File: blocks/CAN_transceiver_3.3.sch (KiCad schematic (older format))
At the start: 0 parts

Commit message: added 4.4v can transciever
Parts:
- added C?: 100n, symbol Device:C
- added U?: SN65HVD232, Package_SO:SOIC-8_3.9x4.9mm_P1.27mm, symbol Interface_CAN_LIN:SN65HVD232
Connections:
- new net +3V3: C?.2, U?.3 (VCC)
- new net CANH: U?.7 (CANH)
- new net CANL: U?.6 (CANL)
- new net GND: C?.1, U?.2 (GND)
- new net RX: U?.4 (R)
- new net TX: U?.1 (D)
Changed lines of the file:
@@
 EESchema Schematic File Version 4
-LIBS:blocks-cache
-EELAYER 29 0
+EELAYER 30 0
 EELAYER END
 $Descr A4 11693 8268
@@
 Comment4 ""
 $EndDescr
+$Comp
+L Interface_CAN_LIN:SN65HVD232 U?
+U 1 1 5EEB2C8B
+P 5500 3000
+F 0 "U?" H 5300 3250 50  0000 C CNN
+F 1 "SN65HVD232" H 5850 2650 50  0000 C CNN
+F 2 "Package_SO:SOIC-8_3.9x4.9mm_P1.27mm" H 5500 2500 50  0001 C CNN
+F 3 "http://www.ti.com/lit/ds/symlink/sn65hvd230.pdf" H 5400 3400 50  0001 C CNN
+	1    5500 3000
+	1    0    0    -1
+$EndComp
+Text HLabel 4700 2900 0    50   Input ~ 0
+TX
+Text HLabel 4700 3000 0    50   Output ~ 0
+RX
+Wire Wire Line
+	4700 2900 5100 2900
+Wire Wire Line
+	5100 3000 4700 3000
+Text HLabel 6350 3000 2    50   BiDi ~ 0
+CANH
+Text HLabel 6350 3100 2    50   BiDi ~ 0
+CANL
+Wire Wire Line
+	5900 3000 6350 3000
+Wire Wire Line
+	6350 3100 5900 3100
+Wire Wire Line
+	5500 2700 5500 2550
+$Comp
+L power:+3.3V #PWR?
+U 1 1 5EEB36C2
+P 5500 2400
+F 0 "#PWR?" H 5500 2250 50  0001 C CNN
+F 1 "+3.3V" H 5515 2573 50  0000 C CNN
+F 2 "" H 5500 2400 50  0001 C CNN
+F 3 "" H 5500 2400 50  0001 C CNN
+	1    5500 2400
+	1    0    0    -1
+$EndComp
+$Comp
+L power:GND #PWR?
+U 1 1 5EEB3802
+P 5500 3500
+F 0 "#PWR?" H 5500 3250 50  0001 C CNN
+F 1 "GND" H 5505 3327 50  0000 C CNN
+F 2 "" H 5500 3500 50  0001 C CNN
+F 3 "" H 5500 3500 50  0001 C CNN
+	1    5500 3500
+	1    0    0    -1
+$EndComp
+Wire Wire Line
+	5500 3500 5500 3400
+$Comp
+L Device:C C?
+U 1 1 5EEB3AF7
+P 5750 2550
+F 0 "C?" V 5498 2550 50  0000 C CNN
+F 1 "100n" V 5589 2550 50  0000 C CNN
+F 2 "" H 5788 2400 50  0001 C CNN
+F 3 "~" H 5750 2550 50  0001 C CNN
+	1    5750 2550
+	0    1    1    0
+$EndComp
+Wire Wire Line
+	5600 2550 5500 2550
+Connection ~ 5500 2550
+Wire Wire Line
+	5500 2550 5500 2400
+$Comp
+L power:GND #PWR?
+U 1 1 5EEB4720
+P 5950 2600
+F 0 "#PWR?" H 5950 2350 50  0001 C CNN
+F 1 "GND" H 5955 2427 50  0000 C CNN
+F 2 "" H 5950 2600 50  0001 C CNN
+F 3 "" H 5950 2600 50  0001 C CNN
+	1    5950 2600
+	1    0    0    -1
+$EndComp
+Wire Wire Line
+	5950 2600 5950 2550
+Wire Wire Line
+	5950 2550 5900 2550
 $EndSCHEMATC

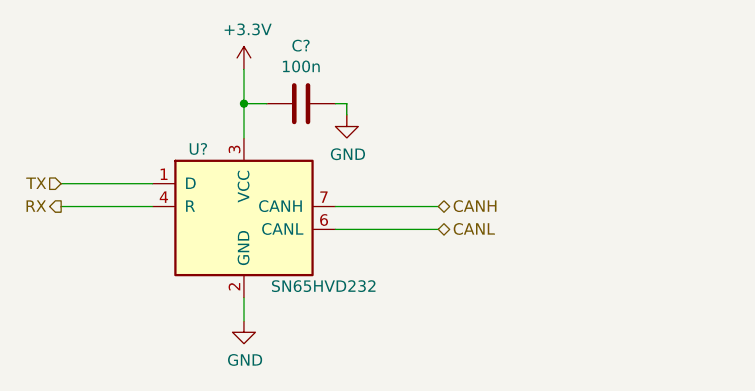
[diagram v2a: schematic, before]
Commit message: changed 3.3 can to sn65hvd233
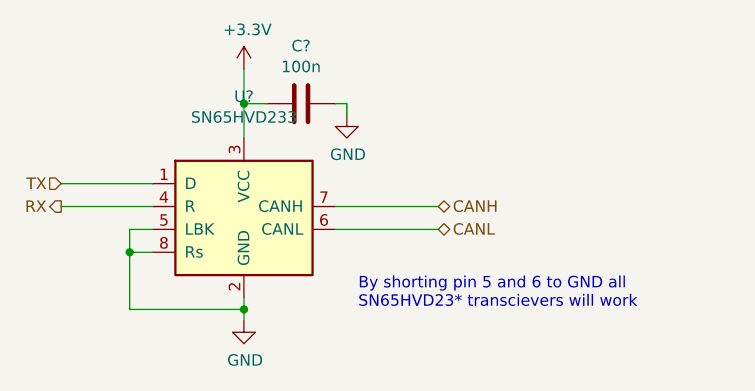
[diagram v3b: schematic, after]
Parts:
- removed U?: SN65HVD232, Package_SO:SOIC-8_3.9x4.9mm_P1.27mm, symbol Interface_CAN_LIN:SN65HVD232
- added U?: SN65HVD233, Package_SO:SOIC-8_3.9x4.9mm_P1.27mm, symbol Interface_CAN_LIN:SN65HVD233
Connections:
- net +3V3: now also U?.3 (VCC)
- net CANH: now also U?.7 (CANH)
- net CANL: now also U?.6 (CANL)
- net GND: now also U?.2 (GND), U?.5 (LBK), U?.8 (Rs)
- net RX: now also U?.4 (R)
- net TX: now also U?.1 (D)
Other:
- note added: "By shorting pin 5 and 6 to GND all\nSN65HVD23* transcievers will work"
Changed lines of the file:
@@
 $Descr A4 11693 8268
 encoding utf-8
-Sheet 5 8
+Sheet 5 9
 Title "Schematic Blocks"
 Date "2019-12-05"
@@
 Comment4 ""
 $EndDescr
-$Comp
-L Interface_CAN_LIN:SN65HVD232 U?
-U 1 1 5EEB2C8B
-P 5500 3000
-F 0 "U?" H 5300 3250 50  0000 C CNN
-F 1 "SN65HVD232" H 5850 2650 50  0000 C CNN
-F 2 "Package_SO:SOIC-8_3.9x4.9mm_P1.27mm" H 5500 2500 50  0001 C CNN
-F 3 "http://www.ti.com/lit/ds/symlink/sn65hvd230.pdf" H 5400 3400 50  0001 C CNN
-	1    5500 3000
-	1    0    0    -1
-$EndComp
 Text HLabel 4700 2900 0    50   Input ~ 0
 TX
@@
 $EndComp
 Wire Wire Line
-	5500 3500 5500 3400
+	5500 3500 5500 3450
 $Comp
 L Device:C C?
@@
 Wire Wire Line
 	5950 2550 5900 2550
+$Comp
+L Interface_CAN_LIN:SN65HVD233 U?
+U 1 1 5FAEC37C
+P 5500 3000
+F 0 "U?" H 5500 3481 50  0000 C CNN
+F 1 "SN65HVD233" H 5500 3390 50  0000 C CNN
+F 2 "Package_SO:SOIC-8_3.9x4.9mm_P1.27mm" H 5500 2500 50  0001 C CNN
+F 3 "http://www.ti.com/lit/ds/symlink/sn65hvd234.pdf" H 5400 3400 50  0001 C CNN
+	1    5500 3000
+	1    0    0    -1
+$EndComp
+Wire Wire Line
+	5100 3200 5000 3200
+Wire Wire Line
+	5000 3450 5500 3450
+Wire Wire Line
+	5000 3200 5000 3450
+Connection ~ 5500 3450
+Wire Wire Line
+	5500 3450 5500 3400
+Wire Wire Line
+	5100 3100 5000 3100
+Wire Wire Line
+	5000 3100 5000 3200
+Connection ~ 5000 3200
+Text Notes 6000 3450 0    50   ~ 0
+By shorting pin 5 and 6 to GND all\nSN65HVD23* transcievers will work
 $EndSCHEMATC

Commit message: Update CAN_transceiver_3.3.sch
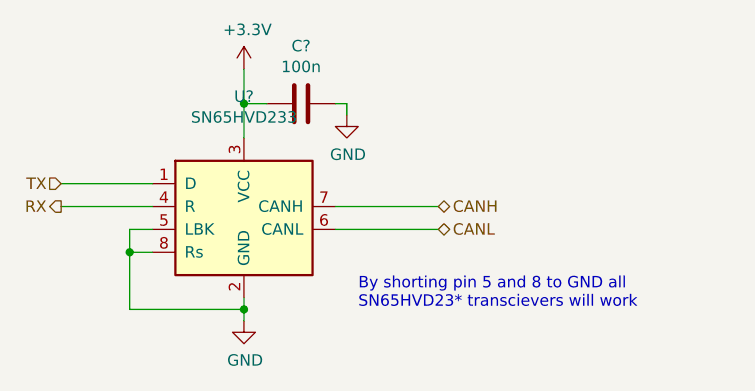
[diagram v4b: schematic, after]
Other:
- note added: "By shorting pin 5 and 8 to GND all\nSN65HVD23* transcievers will work"
- note removed: "By shorting pin 5 and 6 to GND all\nSN65HVD23* transcievers will work"
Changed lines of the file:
@@
 Connection ~ 5000 3200
 Text Notes 6000 3450 0    50   ~ 0
-By shorting pin 5 and 6 to GND all\nSN65HVD23* transcievers will work
+By shorting pin 5 and 8 to GND all\nSN65HVD23* transcievers will work
 $EndSCHEMATC
